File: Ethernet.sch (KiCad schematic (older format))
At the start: 26 parts, among them U5 DM9000B, U6 93LC46, U8 Pulse-J00-0045NL, Y1 25MHz

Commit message: Lotta changes
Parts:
- C44, C45, C46, C47, C48, C49, C51, C53, C54, C55, C56: footprint (none) -> Capacitors_SMD:C_0603
- R10, R11, R12, R13, R14, R15, R16, R17, R9: footprint (none) -> Resistors_SMD:R_0603
- U6: footprint (none) -> Housings_SOIC:SOIC-8_3.9x4.9mm_Pitch1.27mm

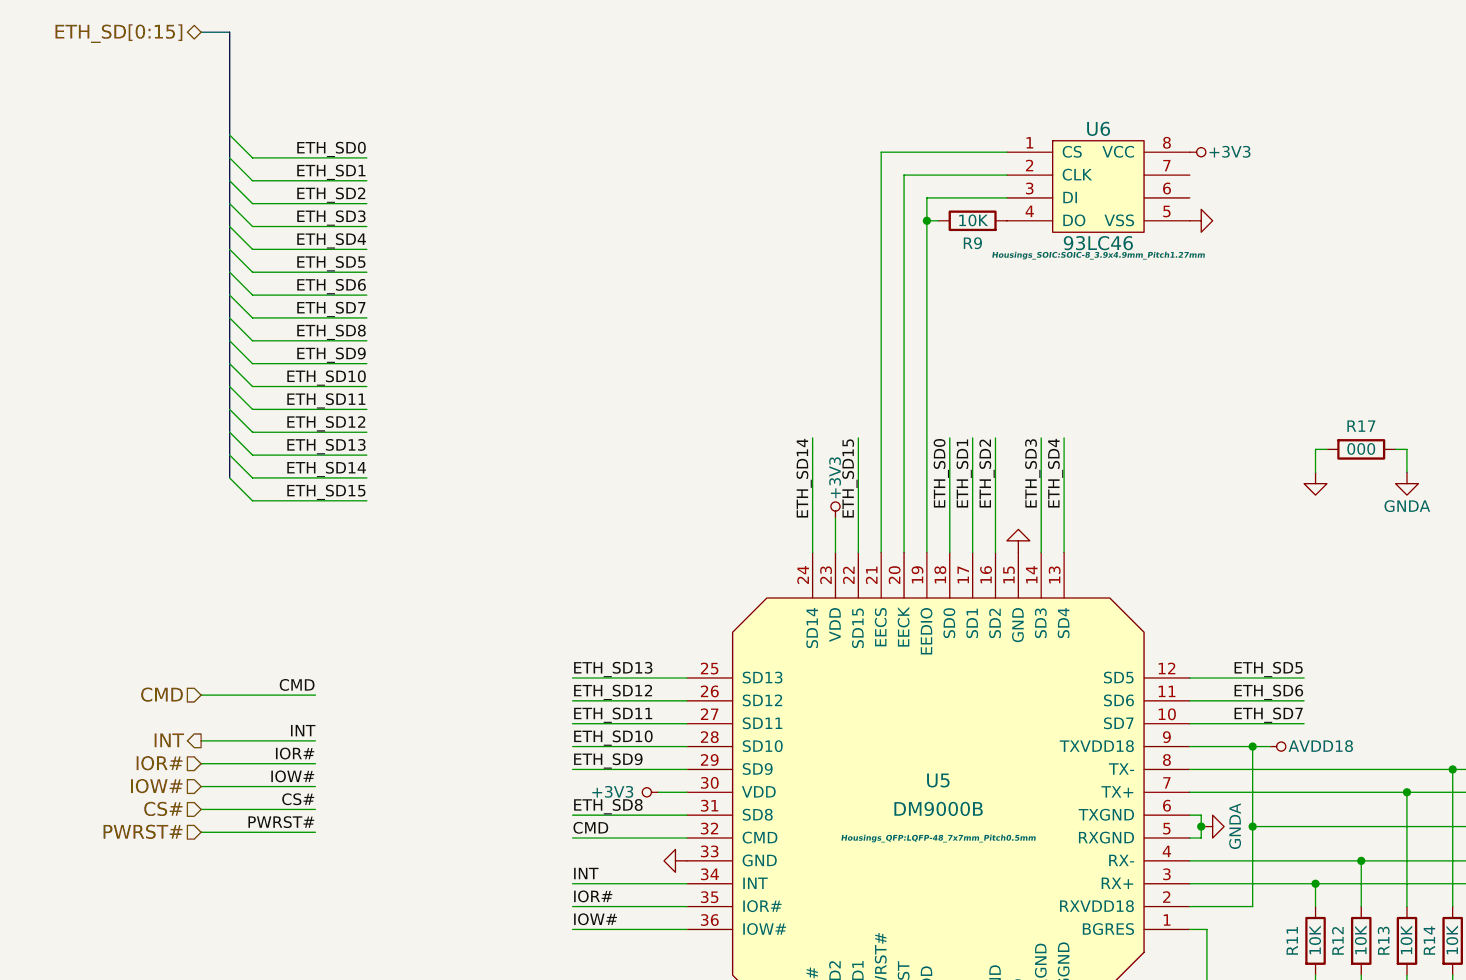
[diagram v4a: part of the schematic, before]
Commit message: Inner layers routing
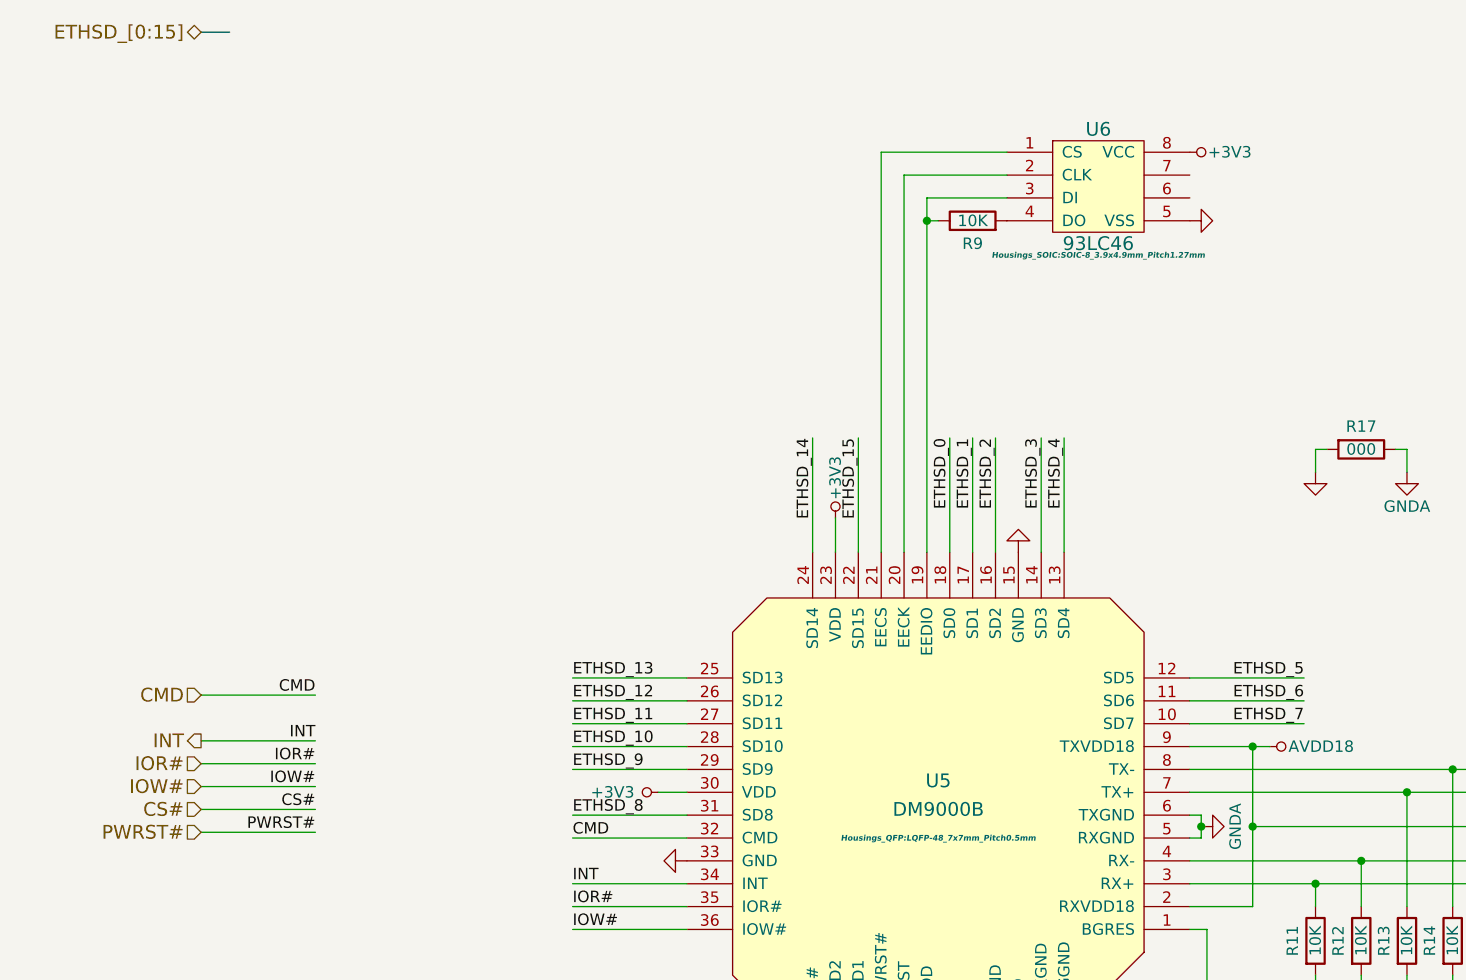
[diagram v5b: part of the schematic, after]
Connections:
- net ETH_SD0 renamed ETHSD_0
- net ETH_SD1 renamed ETHSD_1
- net ETH_SD10 renamed ETHSD_10
- net ETH_SD11 renamed ETHSD_11
- net ETH_SD12 renamed ETHSD_12
- net ETH_SD13 renamed ETHSD_13
- net ETH_SD14 renamed ETHSD_14
- net ETH_SD15 renamed ETHSD_15
- net ETH_SD2 renamed ETHSD_2
- net ETH_SD3 renamed ETHSD_3
- net ETH_SD4 renamed ETHSD_4
- net ETH_SD5 renamed ETHSD_5
- net ETH_SD6 renamed ETHSD_6
- net ETH_SD7 renamed ETHSD_7
- net ETH_SD8 renamed ETHSD_8
- net ETH_SD9 renamed ETHSD_9
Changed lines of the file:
@@
 	4950 5700 4950 5575
 Text Label 3400 3925 0    50   ~ 0
-ETH_SD13
+ETHSD_13
 Wire Wire Line
 	3900 4025 3400 4025
@@
 	3900 4525 3400 4525
 Text Label 3400 4025 0    50   ~ 0
-ETH_SD12
+ETHSD_12
 Text Label 3400 4125 0    50   ~ 0
-ETH_SD11
+ETHSD_11
 Text Label 3400 4225 0    50   ~ 0
-ETH_SD10
+ETHSD_10
 Text Label 3400 4325 0    50   ~ 0
-ETH_SD9
+ETHSD_9
 Text Label 3400 4525 0    50   ~ 0
-ETH_SD8
+ETHSD_8
 Wire Wire Line
 	6100 4225 6450 4225
@@
 Connection ~ 6150 4575
 Text Label 6600 4125 2    50   ~ 0
-ETH_SD7
+ETHSD_7
 Wire Wire Line
 	6100 4025 6600 4025
 Text Label 6600 4025 2    50   ~ 0
-ETH_SD6
+ETHSD_6
 Text Label 6600 3925 2    50   ~ 0
-ETH_SD5
+ETHSD_5
 Wire Wire Line
 	6100 3925 6600 3925
 Wire Wire Line
 	6100 4125 6600 4125
-Text Label 2500 3050 2    50   ~ 0
-ETH_SD14
-Wire Wire Line
-	2000 3050 2500 3050
 Text Label 4650 2875 3    50   ~ 0
-ETH_SD15
+ETHSD_15
 Wire Wire Line
 	4650 3375 4650 2875
 Text Label 5050 2875 3    50   ~ 0
-ETH_SD0
+ETHSD_0
 Wire Wire Line
 	5050 3375 5050 2875
 Text Label 5150 2875 3    50   ~ 0
-ETH_SD1
+ETHSD_1
 Wire Wire Line
 	5150 3375 5150 2875
 Text Label 5250 2875 3    50   ~ 0
-ETH_SD2
+ETHSD_2
 Wire Wire Line
 	5250 3375 5250 2875
 Text Label 5450 2875 3    50   ~ 0
-ETH_SD3
+ETHSD_3
 Wire Wire Line
 	5450 3375 5450 2875
 Text Label 5550 2875 3    50   ~ 0
-ETH_SD4
+ETHSD_4
 Wire Wire Line
 	5550 3375 5550 2875
@@
 NoConn ~ 8000 4325
 Text HLabel 1775 1100 0    60   BiDi ~ 0
-ETH_SD[0:15]
+ETHSD_[0:15]
 Wire Bus Line
 	1775 1100 1900 1100
-Wire Bus Line
-	1900 1100 1900 3050
-Text Label 2500 2950 2    50   ~ 0
-ETH_SD13
-Wire Wire Line
-	2000 2850 2500 2850
-Wire Wire Line
-	2000 2650 2500 2650
-Wire Wire Line
-	2000 2550 2500 2550
-Text Label 2500 2850 2    50   ~ 0
-ETH_SD12
-Text Label 2500 2750 2    50   ~ 0
-ETH_SD11
-Text Label 2500 2650 2    50   ~ 0
-ETH_SD10
-Text Label 2500 2550 2    50   ~ 0
-ETH_SD9
-Wire Wire Line
-	2000 2750 2500 2750
-Wire Wire Line
-	2000 2950 2500 2950
-Entry Wire Line
-	1900 1550 2000 1650
-Entry Wire Line
-	1900 1650 2000 1750
-Entry Wire Line
-	1900 1750 2000 1850
-Entry Wire Line
-	1900 1850 2000 1950
-Entry Wire Line
-	1900 1950 2000 2050
-Entry Wire Line
-	1900 2050 2000 2150
-Entry Wire Line
-	1900 2150 2000 2250
-Entry Wire Line
-	1900 2250 2000 2350
-Entry Wire Line
-	1900 2350 2000 2450
-Entry Wire Line
-	1900 2450 2000 2550
-Entry Wire Line
-	1900 2550 2000 2650
-Entry Wire Line
-	1900 2650 2000 2750
-Entry Wire Line
-	1900 2750 2000 2850
-Entry Wire Line
-	1900 2850 2000 2950
-Entry Wire Line
-	1900 2950 2000 3050
-Entry Wire Line
-	1900 3050 2000 3150
-Text Label 2500 1650 2    50   ~ 0
-ETH_SD0
-Wire Wire Line
-	2000 1650 2500 1650
-Text Label 2500 1750 2    50   ~ 0
-ETH_SD1
-Wire Wire Line
-	2000 1750 2500 1750
-Text Label 2500 1850 2    50   ~ 0
-ETH_SD2
-Wire Wire Line
-	2000 1850 2500 1850
-Text Label 2500 1950 2    50   ~ 0
-ETH_SD3
-Wire Wire Line
-	2000 1950 2500 1950
-Text Label 2500 2050 2    50   ~ 0
-ETH_SD4
-Wire Wire Line
-	2000 2050 2500 2050
-Text Label 2500 2350 2    50   ~ 0
-ETH_SD7
-Wire Wire Line
-	2000 2250 2500 2250
-Text Label 2500 2250 2    50   ~ 0
-ETH_SD6
-Text Label 2500 2150 2    50   ~ 0
-ETH_SD5
-Wire Wire Line
-	2000 2150 2500 2150
-Wire Wire Line
-	2000 2350 2500 2350
-Wire Wire Line
-	2000 2450 2500 2450
-Text Label 2500 2450 2    50   ~ 0
-ETH_SD8
-Text Label 2500 3150 2    50   ~ 0
-ETH_SD15
-Wire Wire Line
-	2000 3150 2500 3150
 Text Label 4450 2875 3    50   ~ 0
-ETH_SD14
+ETHSD_14
 Wire Wire Line
 	4450 3375 4450 2875

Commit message: Ethernet SD bus resolved
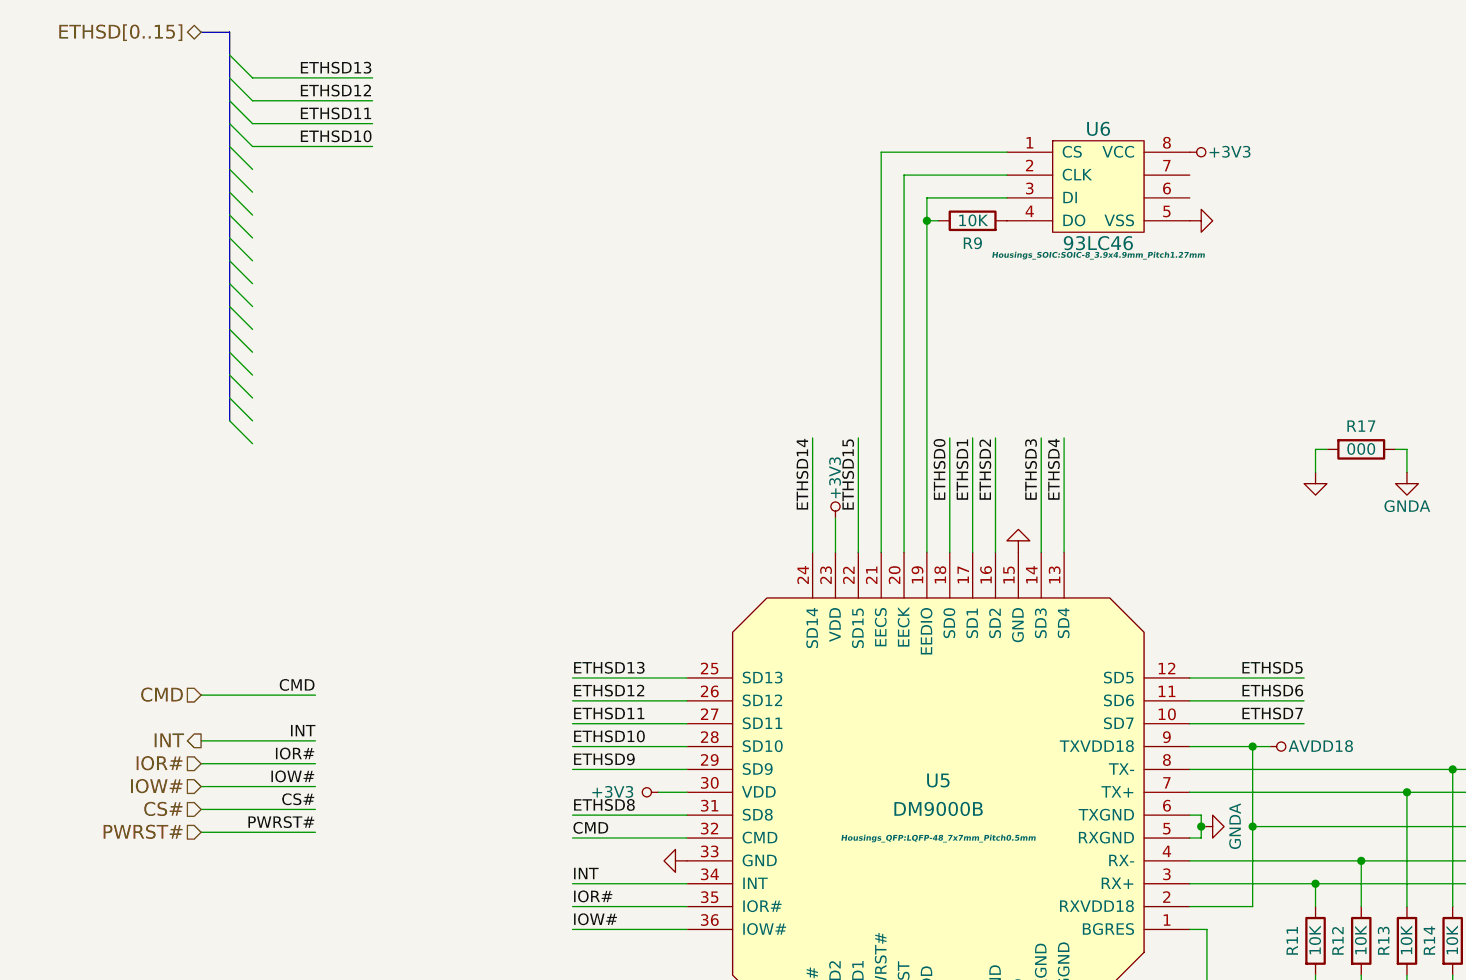
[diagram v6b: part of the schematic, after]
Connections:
- net ETHSD_0 renamed ETHSD0
- net ETHSD_1 renamed ETHSD1
- net ETHSD_10 renamed ETHSD10
- net ETHSD_11 renamed ETHSD11
- net ETHSD_12 renamed ETHSD12
- net ETHSD_13 renamed ETHSD13
- net ETHSD_14 renamed ETHSD14
- net ETHSD_15 renamed ETHSD15
- net ETHSD_2 renamed ETHSD2
- net ETHSD_3 renamed ETHSD3
- net ETHSD_4 renamed ETHSD4
- net ETHSD_5 renamed ETHSD5
- net ETHSD_6 renamed ETHSD6
- net ETHSD_7 renamed ETHSD7
- net ETHSD_8 renamed ETHSD8
- net ETHSD_9 renamed ETHSD9
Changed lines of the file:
@@
 	4950 5700 4950 5575
 Text Label 3400 3925 0    50   ~ 0
-ETHSD_13
+ETHSD13
 Wire Wire Line
 	3900 4025 3400 4025
@@
 	3900 4525 3400 4525
 Text Label 3400 4025 0    50   ~ 0
-ETHSD_12
+ETHSD12
 Text Label 3400 4125 0    50   ~ 0
-ETHSD_11
+ETHSD11
 Text Label 3400 4225 0    50   ~ 0
-ETHSD_10
+ETHSD10
 Text Label 3400 4325 0    50   ~ 0
-ETHSD_9
+ETHSD9
 Text Label 3400 4525 0    50   ~ 0
-ETHSD_8
+ETHSD8
 Wire Wire Line
 	6100 4225 6450 4225
@@
 Connection ~ 6150 4575
 Text Label 6600 4125 2    50   ~ 0
-ETHSD_7
+ETHSD7
 Wire Wire Line
 	6100 4025 6600 4025
 Text Label 6600 4025 2    50   ~ 0
-ETHSD_6
+ETHSD6
 Text Label 6600 3925 2    50   ~ 0
-ETHSD_5
+ETHSD5
 Wire Wire Line
 	6100 3925 6600 3925
@@
 	6100 4125 6600 4125
 Text Label 4650 2875 3    50   ~ 0
-ETHSD_15
+ETHSD15
 Wire Wire Line
 	4650 3375 4650 2875
 Text Label 5050 2875 3    50   ~ 0
-ETHSD_0
+ETHSD0
 Wire Wire Line
 	5050 3375 5050 2875
 Text Label 5150 2875 3    50   ~ 0
-ETHSD_1
+ETHSD1
 Wire Wire Line
 	5150 3375 5150 2875
 Text Label 5250 2875 3    50   ~ 0
-ETHSD_2
+ETHSD2
 Wire Wire Line
 	5250 3375 5250 2875
 Text Label 5450 2875 3    50   ~ 0
-ETHSD_3
+ETHSD3
 Wire Wire Line
 	5450 3375 5450 2875
 Text Label 5550 2875 3    50   ~ 0
-ETHSD_4
+ETHSD4
 Wire Wire Line
 	5550 3375 5550 2875
@@
 NoConn ~ 8000 4325
 Text HLabel 1775 1100 0    60   BiDi ~ 0
-ETHSD_[0:15]
+ETHSD[0..15]
 Wire Bus Line
 	1775 1100 1900 1100
 Text Label 4450 2875 3    50   ~ 0
-ETHSD_14
+ETHSD14
 Wire Wire Line
 	4450 3375 4450 2875
@@
 Wire Wire Line
 	7050 2925 7000 2925
+Wire Bus Line
+	1900 1100 1900 2800
+Entry Wire Line
+	1900 1200 2000 1300
+Entry Wire Line
+	1900 1300 2000 1400
+Entry Wire Line
+	1900 1400 2000 1500
+Entry Wire Line
+	1900 1500 2000 1600
+Entry Wire Line
+	1900 1600 2000 1700
+Entry Wire Line
+	1900 1700 2000 1800
+Entry Wire Line
+	1900 1800 2000 1900
+Entry Wire Line
+	1900 1900 2000 2000
+Wire Wire Line
+	2000 1300 2525 1300
+Wire Wire Line
+	2000 1400 2525 1400
+Wire Wire Line
+	2000 1500 2525 1500
+Wire Wire Line
+	2000 1600 2525 1600
+Text Label 2525 1300 2    50   ~ 0
+ETHSD13
+Text Label 2525 1400 2    50   ~ 0
+ETHSD12
+Text Label 2525 1500 2    50   ~ 0
+ETHSD11
+Text Label 2525 1600 2    50   ~ 0
+ETHSD10
+Entry Wire Line
+	1900 2000 2000 2100
+Entry Wire Line
+	1900 2100 2000 2200
+Entry Wire Line
+	1900 2200 2000 2300
+Entry Wire Line
+	1900 2300 2000 2400
+Entry Wire Line
+	1900 2400 2000 2500
+Entry Wire Line
+	1900 2500 2000 2600
+Entry Wire Line
+	1900 2600 2000 2700
+Entry Wire Line
+	1900 2700 2000 2800
+Entry Wire Line
+	1900 2800 2000 2900
 $EndSCHEMATC

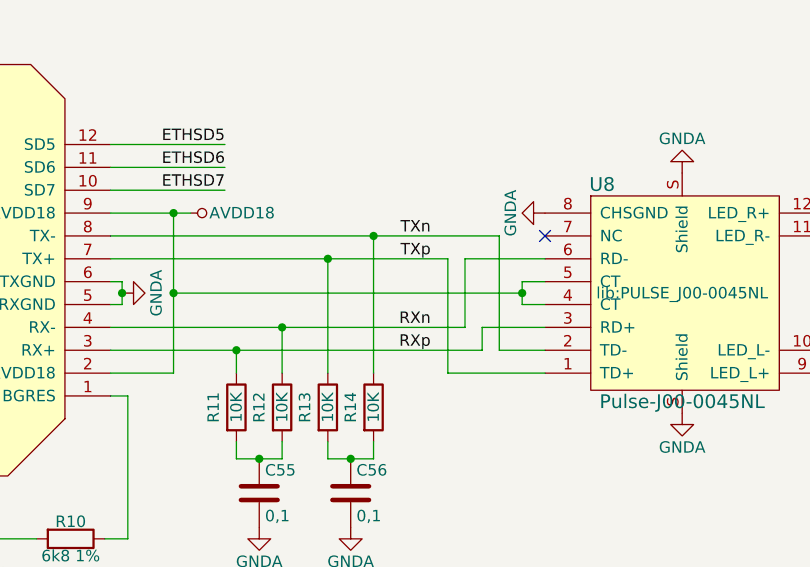
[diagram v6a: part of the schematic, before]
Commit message: More eth stuff
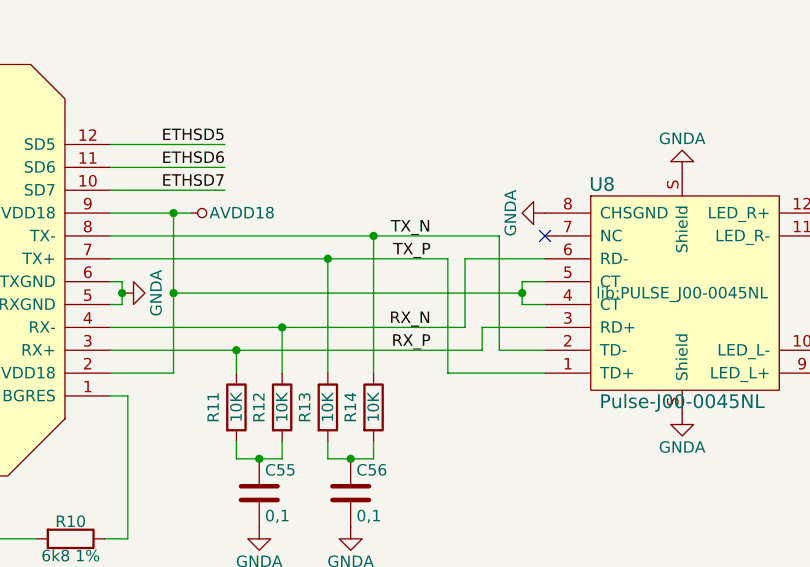
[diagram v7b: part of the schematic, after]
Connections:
- net RXn renamed RX_N
- net RXp renamed RX_P
- net TXn renamed TX_N
- net TXp renamed TX_P
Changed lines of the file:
@@
 Connection ~ 7250 4325
 Text Label 7500 4325 2    50   ~ 0
-TXn
+TX_N
 Text Label 7500 4425 2    50   ~ 0
-TXp
+TX_P
 Text Label 7500 4725 2    50   ~ 0
-RXn
+RX_N
 Text Label 7500 4825 2    50   ~ 0
-RXp
+RX_P
 Wire Wire Line
 	6375 4575 7900 4575
